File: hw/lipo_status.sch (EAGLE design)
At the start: 36 parts, among them IC1 LM317-3V3

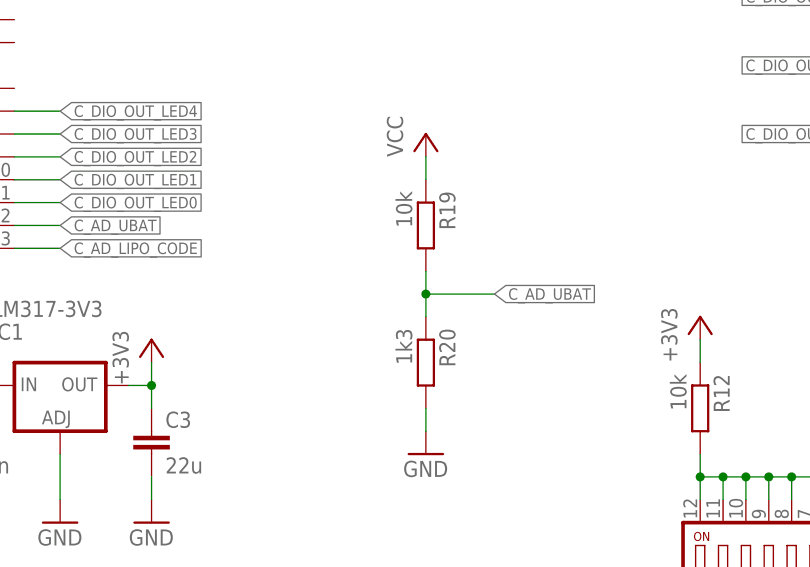
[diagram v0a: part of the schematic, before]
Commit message: removed tracking of eagle backup files\nadapted SW\nadapted schematic and layout
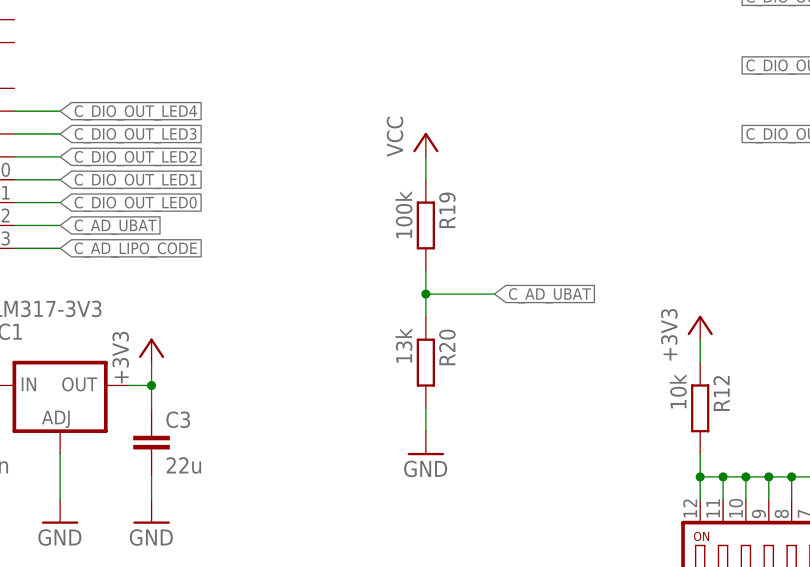
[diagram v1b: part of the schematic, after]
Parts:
- R19: value 10k -> 100k
- R20: value 1k3 -> 13k
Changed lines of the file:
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@@
 <part name="TP1" library="testpad" deviceset="TPSQ" device="PAD1-13"/>
 <part name="TP2" library="testpad" deviceset="TPSQ" device="PAD1-13"/>
-<part name="R19" library="rcl" deviceset="R-EU_" device="R0603" value="10k"/>
-<part name="R20" library="rcl" deviceset="R-EU_" device="R0603" value="1k3"/>
+<part name="R19" library="rcl" deviceset="R-EU_" device="R0603" value="100k"/>
+<part name="R20" library="rcl" deviceset="R-EU_" device="R0603" value="13k"/>
 <part name="P+3" library="supply1" deviceset="VCC" device=""/>
 <part name="GND9" library="supply1" deviceset="GND" device=""/>

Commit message: added gerber files
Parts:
- added R21: 10k, rcl:R-EU_R0603
- added T1: IRLML5203TRPBF, SchlegelAr_Master:IRLML5203TRPBF
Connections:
- new net N$19: R21.1, T1.G
- new net N$20: C2.1, IC1.IN, T1.S
- net GND: now also R21.2
- net VCC: now also T1.D; no longer C2.1, IC1.IN
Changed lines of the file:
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@@
 <part name="C3" library="rcl" deviceset="C-EU" device="C0805" value="22u"/>
 <part name="IC1" library="v-reg" deviceset="LM317?*" device="MBSTT3" value="LM317-3V3"/>
-<part name="P+2" library="supply1" deviceset="VCC" device=""/>
 <part name="+3V3" library="supply1" deviceset="+3V3" device=""/>
 <part name="GND6" library="supply1" deviceset="GND" device=""/>
@@
 <part name="P+3" library="supply1" deviceset="VCC" device=""/>
 <part name="GND9" library="supply1" deviceset="GND" device=""/>
+<part name="T1" library="SchlegelAr_Master" deviceset="IRLML5203TRPBF" device=""/>
+<part name="GND10" library="supply1" deviceset="GND" device=""/>
+<part name="R21" library="rcl" deviceset="R-EU_" device="R0603" value="10k"/>
 </parts>
 <sheets>
@@
 <instance part="R17" gate="G$1" x="177.8" y="137.16"/>
 <instance part="JP2" gate="A" x="33.02" y="96.52" rot="R180"/>
-<instance part="P+1" gate="VCC" x="40.64" y="111.76"/>
+<instance part="P+1" gate="VCC" x="40.64" y="116.84"/>
 <instance part="GND5" gate="1" x="40.64" y="78.74"/>
 <instance part="C1" gate="G$1" x="12.7" y="139.7"/>
@@
 <attribute name="VALUE" x="71.12" y="116.84" size="1.778" layer="96"/>
 </instance>
-<instance part="P+2" gate="VCC" x="66.04" y="114.3"/>
 <instance part="+3V3" gate="G$1" x="88.9" y="114.3"/>
-<instance part="GND6" gate="1" x="66.04" y="93.98"/>
-<instance part="GND7" gate="1" x="78.74" y="93.98"/>
-<instance part="GND8" gate="1" x="88.9" y="93.98"/>
+<instance part="GND6" gate="1" x="66.04" y="78.74"/>
+<instance part="GND7" gate="1" x="78.74" y="78.74"/>
+<instance part="GND8" gate="1" x="88.9" y="78.74"/>
 <instance part="R18" gate="G$1" x="76.2" y="162.56" rot="R270"/>
 <instance part="+3V4" gate="G$1" x="76.2" y="172.72"/>
@@
 <instance part="P+3" gate="VCC" x="119.38" y="137.16"/>
 <instance part="GND9" gate="1" x="119.38" y="101.6"/>
+<instance part="T1" gate="G$1" x="50.8" y="109.22" rot="MR90"/>
+<instance part="GND10" gate="1" x="53.34" y="78.74"/>
+<instance part="R21" gate="G$1" x="53.34" y="93.98" rot="R270"/>
 </instances>
 <busses>
@@
 <segment>
 <pinref part="C2" gate="G$1" pin="2"/>
-<wire x1="66.04" y1="99.06" x2="66.04" y2="96.52" width="0.1524" layer="91"/>
+<wire x1="66.04" y1="99.06" x2="66.04" y2="81.28" width="0.1524" layer="91"/>
 <pinref part="GND6" gate="1" pin="GND"/>
 </segment>
 <segment>
 <pinref part="IC1" gate="G$1" pin="ADJ"/>
-<wire x1="78.74" y1="101.6" x2="78.74" y2="96.52" width="0.1524" layer="91"/>
+<wire x1="78.74" y1="101.6" x2="78.74" y2="81.28" width="0.1524" layer="91"/>
 <pinref part="GND7" gate="1" pin="GND"/>
 </segment>
@@
 <pinref part="C3" gate="G$1" pin="2"/>
 <pinref part="GND8" gate="1" pin="GND"/>
-<wire x1="88.9" y1="96.52" x2="88.9" y2="99.06" width="0.1524" layer="91"/>
+<wire x1="88.9" y1="81.28" x2="88.9" y2="99.06" width="0.1524" layer="91"/>
 </segment>
 <segment>
@@
 <pinref part="GND9" gate="1" pin="GND"/>
 <wire x1="119.38" y1="106.68" x2="119.38" y2="104.14" width="0.1524" layer="91"/>
+</segment>
+<segment>
+<pinref part="GND10" gate="1" pin="GND"/>
+<pinref part="R21" gate="G$1" pin="2"/>
+<wire x1="53.34" y1="81.28" x2="53.34" y2="88.9" width="0.1524" layer="91"/>
 </segment>
 </net>
@@
 <wire x1="40.64" y1="101.6" x2="40.64" y2="104.14" width="0.1524" layer="91"/>
 <wire x1="40.64" y1="104.14" x2="40.64" y2="109.22" width="0.1524" layer="91"/>
+<wire x1="40.64" y1="109.22" x2="40.64" y2="114.3" width="0.1524" layer="91"/>
 <wire x1="35.56" y1="93.98" x2="40.64" y2="93.98" width="0.1524" layer="91"/>
 <junction x="40.64" y="93.98"/>
@@
 <wire x1="35.56" y1="104.14" x2="40.64" y2="104.14" width="0.1524" layer="91"/>
 <junction x="40.64" y="104.14"/>
-</segment>
-<segment>
-<pinref part="IC1" gate="G$1" pin="IN"/>
-<pinref part="C2" gate="G$1" pin="1"/>
-<wire x1="71.12" y1="109.22" x2="66.04" y2="109.22" width="0.1524" layer="91"/>
-<wire x1="66.04" y1="109.22" x2="66.04" y2="106.68" width="0.1524" layer="91"/>
-<junction x="66.04" y="109.22"/>
-<wire x1="66.04" y1="109.22" x2="66.04" y2="111.76" width="0.1524" layer="91"/>
-<pinref part="P+2" gate="VCC" pin="VCC"/>
+<pinref part="T1" gate="G$1" pin="D"/>
+<wire x1="45.72" y1="109.22" x2="40.64" y2="109.22" width="0.1524" layer="91"/>
+<junction x="40.64" y="109.22"/>
 </segment>
 <segment>
@@
 </segment>
 </net>
+<net name="N$19" class="0">
+<segment>
+<pinref part="T1" gate="G$1" pin="G"/>
+<pinref part="R21" gate="G$1" pin="1"/>
+<wire x1="53.34" y1="99.06" x2="53.34" y2="104.14" width="0.1524" layer="91"/>
+</segment>
+</net>
+<net name="N$20" class="0">
+<segment>
+<pinref part="T1" gate="G$1" pin="S"/>
+<pinref part="IC1" gate="G$1" pin="IN"/>
+<wire x1="55.88" y1="109.22" x2="66.04" y2="109.22" width="0.1524" layer="91"/>
+<pinref part="C2" gate="G$1" pin="1"/>
+<wire x1="66.04" y1="109.22" x2="71.12" y2="109.22" width="0.1524" layer="91"/>
+<wire x1="66.04" y1="106.68" x2="66.04" y2="109.22" width="0.1524" layer="91"/>
+<junction x="66.04" y="109.22"/>
+</segment>
+</net>
